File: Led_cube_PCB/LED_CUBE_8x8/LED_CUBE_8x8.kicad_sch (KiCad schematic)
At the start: 0 parts

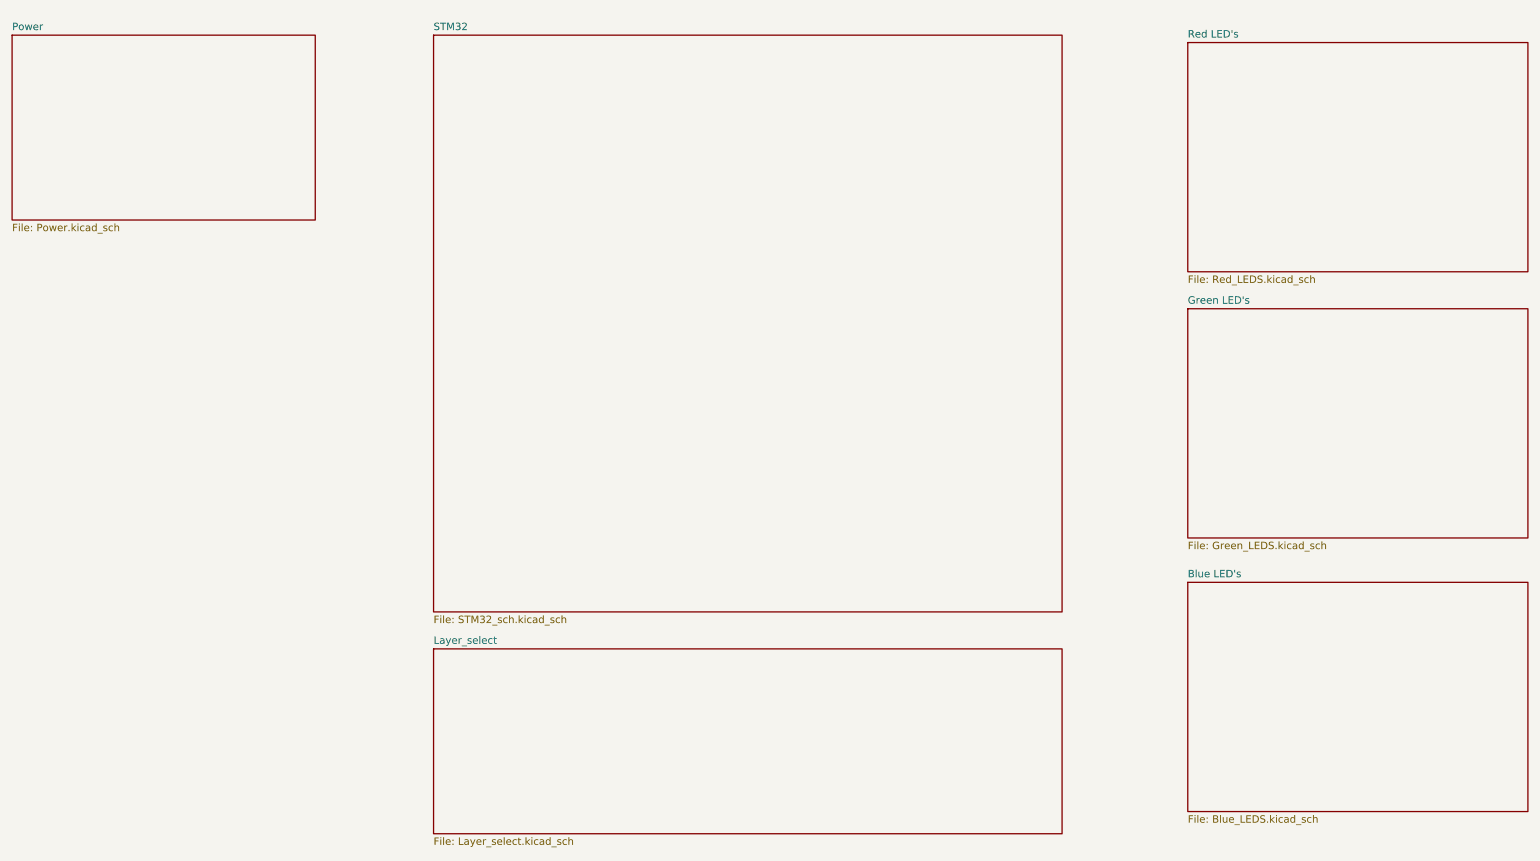
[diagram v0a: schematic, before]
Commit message: Finalized schematic changed power source and buck converter due to unavailability stock mouser. Also assigned all the footprints to all components and ran ERC.
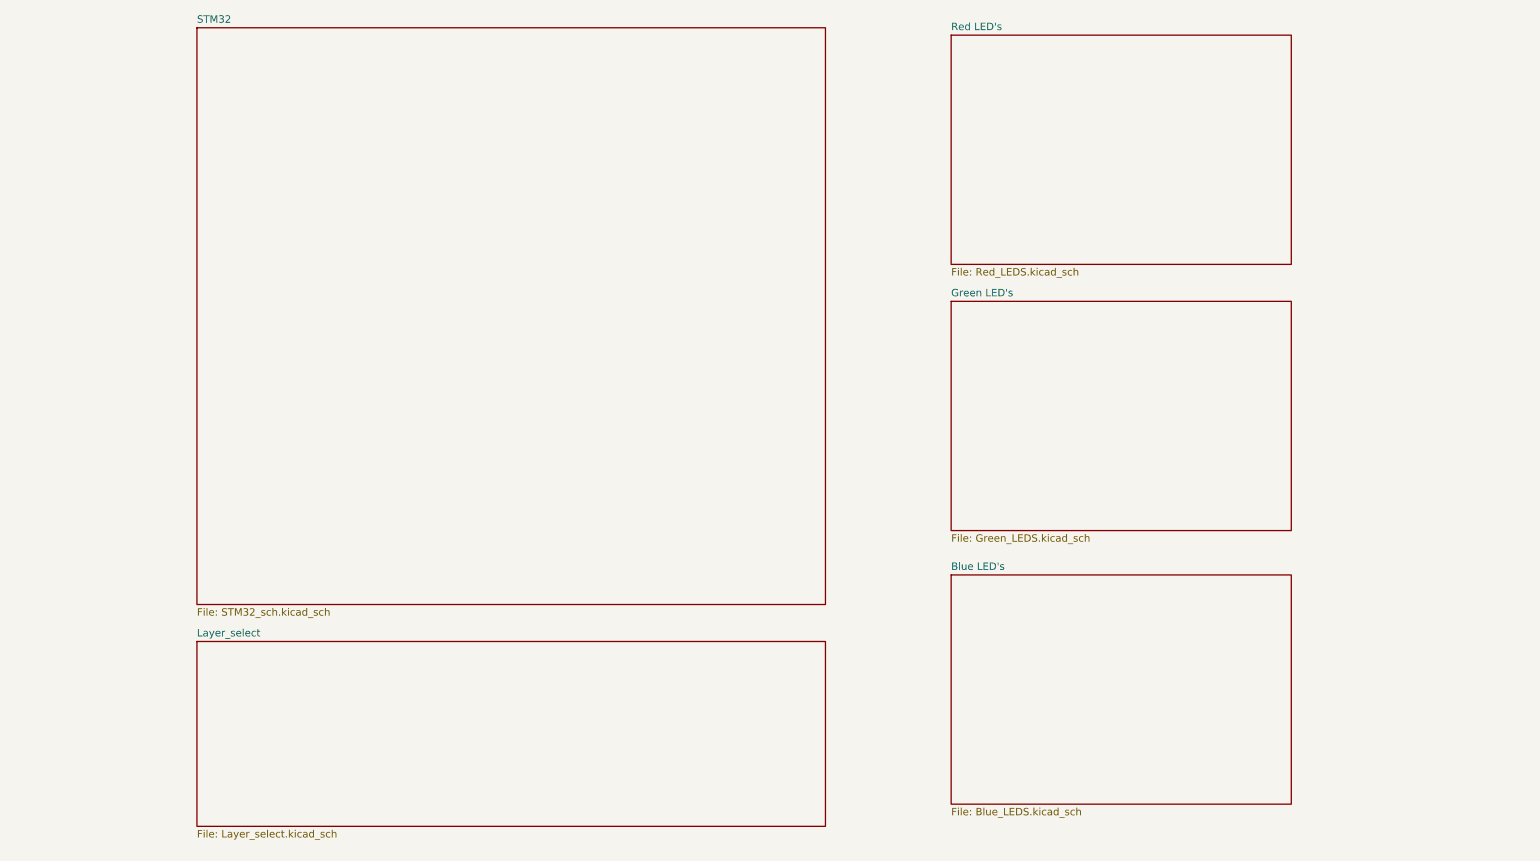
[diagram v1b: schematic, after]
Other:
- removed sheet Power
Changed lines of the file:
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@@
 	)
 	(sheet
-		(at 223.52 69.85)
+		(at 182.88 68.58)
 		(size 58.42 39.37)
 		(exclude_from_sim no)
@@
 		)
 		(property "Sheetname" "Green LED's"
-			(at 223.52 69.1384 0)
+			(at 182.88 67.8684 0)
 			(show_name no)
 			(do_not_autoplace no)
@@
 		)
 		(property "Sheetfile" "Green_LEDS.kicad_sch"
-			(at 223.52 109.8046 0)
+			(at 182.88 108.5346 0)
 			(show_name no)
 			(do_not_autoplace no)
@@
 	)
 	(sheet
-		(at 223.52 24.13)
+		(at 182.88 22.86)
 		(size 58.42 39.37)
 		(exclude_from_sim no)
@@
 		)
 		(property "Sheetname" "Red LED's"
-			(at 223.52 23.4184 0)
+			(at 182.88 22.1484 0)
 			(show_name no)
 			(do_not_autoplace no)
@@
 		)
 		(property "Sheetfile" "Red_LEDS.kicad_sch"
-			(at 223.52 64.0846 0)
+			(at 182.88 62.8146 0)
 			(show_name no)
 			(do_not_autoplace no)
@@
 	)
 	(sheet
-		(at 93.98 22.86)
+		(at 53.34 21.59)
 		(size 107.95 99.06)
 		(exclude_from_sim no)
@@
 		)
 		(property "Sheetname" "STM32"
-			(at 93.98 22.1484 0)
+			(at 53.34 20.8784 0)
 			(show_name no)
 			(do_not_autoplace no)
@@
 		)
 		(property "Sheetfile" "STM32_sch.kicad_sch"
-			(at 93.98 122.5046 0)
+			(at 53.34 121.2346 0)
 			(show_name no)
 			(do_not_autoplace no)
@@
 	)
 	(sheet
-		(at 93.98 128.27)
+		(at 53.34 127)
 		(size 107.95 31.75)
 		(exclude_from_sim no)
@@
 		)
 		(property "Sheetname" "Layer_select"
-			(at 93.98 127.5584 0)
+			(at 53.34 126.2884 0)
 			(show_name no)
 			(do_not_autoplace no)
@@
 		)
 		(property "Sheetfile" "Layer_select.kicad_sch"
-			(at 93.98 160.6046 0)
+			(at 53.34 159.3346 0)
 			(show_name no)
 			(do_not_autoplace no)
@@
 	)
 	(sheet
-		(at 223.52 116.84)
+		(at 182.88 115.57)
 		(size 58.42 39.37)
 		(exclude_from_sim no)
@@
 		)
 		(property "Sheetname" "Blue LED's"
-			(at 223.52 116.1284 0)
+			(at 182.88 114.8584 0)
 			(show_name no)
 			(do_not_autoplace no)
@@
 		)
 		(property "Sheetfile" "Blue_LEDS.kicad_sch"
-			(at 223.52 156.7946 0)
+			(at 182.88 155.5246 0)
 			(show_name no)
 			(do_not_autoplace no)
@@
 				)
 			)
-		)
-	)
-	(sheet
-		(at 21.59 22.86)
-		(size 52.07 31.75)
-		(exclude_from_sim no)
-		(in_bom yes)
-		(on_board yes)
-		(dnp no)
-		(fields_autoplaced yes)
-		(stroke
-			(width 0.1524)
-			(type solid)
-		)
-		(fill
-			(color 0 0 0 0)
-		)
-		(property "Sheetname" "Power"
-			(at 21.59 22.1484 0)
-			(show_name no)
-			(do_not_autoplace no)
-			(effects
-				(font
-					(size 1.27 1.27)
-				)
-				(justify left bottom)
-			)
-		)
-		(property "Sheetfile" "Power.kicad_sch"
-			(at 21.59 55.1946 0)
-			(show_name no)
-			(do_not_autoplace no)
-			(effects
-				(font
-					(size 1.27 1.27)
-				)
-				(justify left top)
-			)
-		)
-		(instances
-			(project "LED_CUBE_8x8"
-				(path "/b239677e-e361-4439-8200-63fb41f7e03c"
-					(page "5")
-				)
-			)
